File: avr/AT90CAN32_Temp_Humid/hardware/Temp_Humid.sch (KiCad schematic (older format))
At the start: 17 parts, among them P1 CONN_3X2, P2 CONN_4, P3 CONN_4, U1 DS1820, U2 AT90CAN32, U3 7805, U4 MCP2551, X1 16MHz

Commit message: Finilized HIH4000 humdity reading and reviewed PCB before paper print
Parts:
- removed P?: CONN_2, symbol CONN_2
- added K1: CONN_3, symbol CONN_3
- added SW1: SW_PUSH, symbol SW_PUSH
- added U5: HIH4000, symbol DS1820
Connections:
- wire segments 92 -> 114
- no-connect marks 49 -> 46
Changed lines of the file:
@@
 LIBS:contrib
 LIBS:valves
-LIBS:CAN_Temp-cache
+LIBS:Temp_Humid-cache
 EELAYER 27 0
 EELAYER END
@@
 Sheet 1 1
 Title ""
-Date "17 oct 2014"
+Date "20 oct 2014"
 Rev ""
 Comp ""
@@
 NoConn ~ 6500 3900
 NoConn ~ 6500 4000
-NoConn ~ 6500 4150
 NoConn ~ 6500 4250
 NoConn ~ 6500 4350
@@
 NoConn ~ 4550 4350
 NoConn ~ 4550 4250
-NoConn ~ 4550 4150
 NoConn ~ 4550 4000
 NoConn ~ 4550 3900
@@
 $EndComp
 $Comp
-L +5V #PWR01
+L +5V #PWR5
 U 1 1 00000000
 P 3450 1700
-F 0 "#PWR01" H 3450 1790 20  0001 C CNN
+F 0 "#PWR5" H 3450 1790 20  0001 C CNN
 F 1 "+5V" H 3450 1790 30  0000 C CNN
 F 2 "" H 3450 1700 60  0001 C CNN
@@
 $EndComp
 $Comp
-L GND #PWR02
+L GND #PWR2
 U 1 1 52152F91
 P 2850 2300
-F 0 "#PWR02" H 2850 2300 30  0001 C CNN
+F 0 "#PWR2" H 2850 2300 30  0001 C CNN
 F 1 "GND" H 2850 2230 30  0001 C CNN
 F 2 "" H 2850 2300 60  0001 C CNN
@@
 $EndComp
 $Comp
-L +5V #PWR03
+L +5V #PWR1
 U 1 1 52152F8D
 P 2600 3650
-F 0 "#PWR03" H 2600 3740 20  0001 C CNN
+F 0 "#PWR1" H 2600 3740 20  0001 C CNN
 F 1 "+5V" H 2600 3740 30  0000 C CNN
 F 2 "" H 2600 3650 60  0001 C CNN
@@
 $EndComp
 $Comp
-L GND #PWR04
+L GND #PWR4
 U 1 1 52152F8B
 P 3150 4350
-F 0 "#PWR04" H 3150 4350 30  0001 C CNN
+F 0 "#PWR4" H 3150 4350 30  0001 C CNN
 F 1 "GND" H 3150 4280 30  0001 C CNN
 F 2 "" H 3150 4350 60  0001 C CNN
@@
 $EndComp
 $Comp
-L +5V #PWR05
+L +5V #PWR6
 U 1 1 52152F8A
 P 3600 4000
-F 0 "#PWR05" H 3600 4090 20  0001 C CNN
+F 0 "#PWR6" H 3600 4090 20  0001 C CNN
 F 1 "+5V" H 3600 4090 30  0000 C CNN
 F 2 "" H 3600 4000 60  0001 C CNN
@@
 $EndComp
 $Comp
-L +5V #PWR06
+L +5V #PWR8
 U 1 1 52152F74
 P 5550 1750
-F 0 "#PWR06" H 5550 1840 20  0001 C CNN
+F 0 "#PWR8" H 5550 1840 20  0001 C CNN
 F 1 "+5V" H 5550 1840 30  0000 C CNN
 F 2 "" H 5550 1750 60  0001 C CNN
@@
 $EndComp
 $Comp
-L GND #PWR07
+L GND #PWR9
 U 1 1 52152F83
 P 5800 6250
-F 0 "#PWR07" H 5800 6250 30  0001 C CNN
+F 0 "#PWR9" H 5800 6250 30  0001 C CNN
 F 1 "GND" H 5800 6180 30  0001 C CNN
 F 2 "" H 5800 6250 60  0001 C CNN
 F 3 "" H 5800 6250 60  0001 C CNN
 	1    5800 6250
-	1    0    0    -1
-$EndComp
-NoConn ~ 8250 3850
-$Comp
-L GND #PWR08
-U 1 1 52152F82
-P 6950 4150
-F 0 "#PWR08" H 6950 4150 30  0001 C CNN
-F 1 "GND" H 6950 4080 30  0001 C CNN
-F 2 "" H 6950 4150 60  0001 C CNN
-F 3 "" H 6950 4150 60  0001 C CNN
-	1    6950 4150
 	1    0    0    -1
 $EndComp
@@
 $EndComp
 $Comp
-L +5V #PWR09
+L +5V #PWR10
 U 1 1 52152F7D
 P 6750 1150
-F 0 "#PWR09" H 6750 1240 20  0001 C CNN
+F 0 "#PWR10" H 6750 1240 20  0001 C CNN
 F 1 "+5V" H 6750 1240 30  0000 C CNN
 F 2 "" H 6750 1150 60  0001 C CNN
@@
 $EndComp
 $Comp
-L GND #PWR010
+L GND #PWR12
 U 1 1 52152F7C
 P 7700 1900
-F 0 "#PWR010" H 7700 1900 30  0001 C CNN
+F 0 "#PWR12" H 7700 1900 30  0001 C CNN
 F 1 "GND" H 7700 1830 30  0001 C CNN
 F 2 "" H 7700 1900 60  0001 C CNN
@@
 $EndComp
 $Comp
-L +12V #PWR011
+L +12V #PWR14
 U 1 1 52152F79
 P 8900 1050
-F 0 "#PWR011" H 8900 1000 20  0001 C CNN
+F 0 "#PWR14" H 8900 1000 20  0001 C CNN
 F 1 "+12V" H 8900 1150 30  0000 C CNN
 F 2 "" H 8900 1050 60  0001 C CNN
@@
 $EndComp
 $Comp
-L GND #PWR012
+L GND #PWR13
 U 1 1 52152F78
 P 8750 5050
-F 0 "#PWR012" H 8750 5050 30  0001 C CNN
+F 0 "#PWR13" H 8750 5050 30  0001 C CNN
 F 1 "GND" H 8750 4980 30  0001 C CNN
 F 2 "" H 8750 5050 60  0001 C CNN
@@
 	3000 2050 3000 1900
 Wire Wire Line
-	3100 2450 4550 2450
-Wire Wire Line
 	3900 4550 3750 4550
 Connection ~ 3050 4700
@@
 	2600 3650 2600 3950
 Wire Wire Line
-	3100 2450 3100 1900
+	3100 1900 3100 2750
 Wire Wire Line
 	3200 1900 3200 2050
@@
 Wire Wire Line
 	3700 2350 3700 2450
-Connection ~ 3700 2450
 Wire Wire Line
 	5800 5950 5800 6250
@@
 	8100 1300 8100 1250
 $Comp
-L GND #PWR013
+L GND #PWR3
 U 1 1 52BCB805
 P 2900 5750
-F 0 "#PWR013" H 2900 5750 30  0001 C CNN
+F 0 "#PWR3" H 2900 5750 30  0001 C CNN
 F 1 "GND" H 2900 5680 30  0001 C CNN
 F 2 "" H 2900 5750 60  0000 C CNN
@@
 	2900 3850 2600 3850
 Connection ~ 2600 3850
-$Comp
-L CONN_2 P?
-U 1 1 544180F6
+NoConn ~ 6500 2850
+Wire Wire Line
+	6850 2750 6500 2750
+Wire Wire Line
+	6800 2650 6500 2650
+Wire Wire Line
+	8250 3850 8400 3850
+Wire Wire Line
+	8400 3850 8400 4750
+Wire Wire Line
+	8400 4750 8750 4750
+Connection ~ 8750 4750
+Wire Wire Line
+	6950 4150 8400 4150
+Connection ~ 8400 4150
+Wire Wire Line
+	4550 4150 3950 4150
+Wire Wire Line
+	3950 4150 3950 2750
+Wire Wire Line
+	3950 2750 3100 2750
+$Comp
+L SW_PUSH SW1
+U 1 1 54418504
+P 4250 2050
+F 0 "SW1" H 4400 2160 50  0000 C CNN
+F 1 "SW_PUSH" H 4250 1970 50  0000 C CNN
+F 2 "" H 4250 2050 60  0000 C CNN
+F 3 "" H 4250 2050 60  0000 C CNN
+	1    4250 2050
+	0    -1   -1   0
+$EndComp
+$Comp
+L GND #PWR7
+U 1 1 54418511
+P 4650 1800
+F 0 "#PWR7" H 4650 1800 30  0001 C CNN
+F 1 "GND" H 4650 1730 30  0001 C CNN
+F 2 "" H 4650 1800 60  0001 C CNN
+F 3 "" H 4650 1800 60  0001 C CNN
+	1    4650 1800
+	1    0    0    -1
+$EndComp
+Wire Wire Line
+	4550 2450 4250 2450
+Wire Wire Line
+	4250 2450 4250 2350
+Wire Wire Line
+	4250 1750 4250 1550
+Wire Wire Line
+	4250 1550 4650 1550
+Wire Wire Line
+	4650 1550 4650 1800
+Wire Wire Line
+	3700 2450 3100 2450
+Connection ~ 3100 2450
+$Comp
+L DS1820 U5
+U 1 1 54456AA5
+P 7250 5000
+F 0 "U5" H 7250 4300 60  0000 C CNN
+F 1 "HIH4000" H 7250 5000 60  0000 C CNN
+F 2 "" H 7250 5000 60  0000 C CNN
+F 3 "" H 7250 5000 60  0000 C CNN
+	1    7250 5000
+	-1   0    0    1
+$EndComp
+Wire Wire Line
+	6500 4150 6850 4150
+Wire Wire Line
+	6850 4150 6850 4300
+Wire Wire Line
+	6850 4300 7250 4300
+Wire Wire Line
+	7250 4300 7250 4450
+Wire Wire Line
+	7350 4450 8400 4450
+Connection ~ 8400 4450
+$Comp
+L +5V #PWR11
+U 1 1 54456BCE
+P 6800 4600
+F 0 "#PWR11" H 6800 4690 20  0001 C CNN
+F 1 "+5V" H 6800 4690 30  0000 C CNN
+F 2 "" H 6800 4600 60  0001 C CNN
+F 3 "" H 6800 4600 60  0001 C CNN
+	1    6800 4600
+	1    0    0    -1
+$EndComp
+Wire Wire Line
+	7150 4450 6950 4450
+Wire Wire Line
+	6950 4450 6950 4750
+Wire Wire Line
+	6950 4750 6800 4750
+Wire Wire Line
+	6800 4750 6800 4600
+$Comp
+L CONN_3 K1
+U 1 1 544570D5
 P 7500 2550
-F 0 "P?" V 7450 2550 40  0000 C CNN
-F 1 "CONN_2" V 7550 2550 40  0000 C CNN
+F 0 "K1" V 7450 2550 50  0000 C CNN
+F 1 "CONN_3" V 7550 2550 40  0000 C CNN
 F 2 "" H 7500 2550 60  0000 C CNN
 F 3 "" H 7500 2550 60  0000 C CNN
@@
 $EndComp
 Wire Wire Line
-	6800 2450 7150 2450
-Wire Wire Line
-	6850 2650 7150 2650
-NoConn ~ 6500 2850
+	7150 2650 6850 2650
 Wire Wire Line
 	6850 2650 6850 2750
 Wire Wire Line
-	6850 2750 6500 2750
-Wire Wire Line
-	6800 2450 6800 2650
-Wire Wire Line
-	6800 2650 6500 2650
+	7150 2550 6800 2550
+Wire Wire Line
+	6800 2550 6800 2650
+Wire Wire Line
+	7150 2450 7150 1700
+Connection ~ 7150 1700
 $EndSCHEMATC

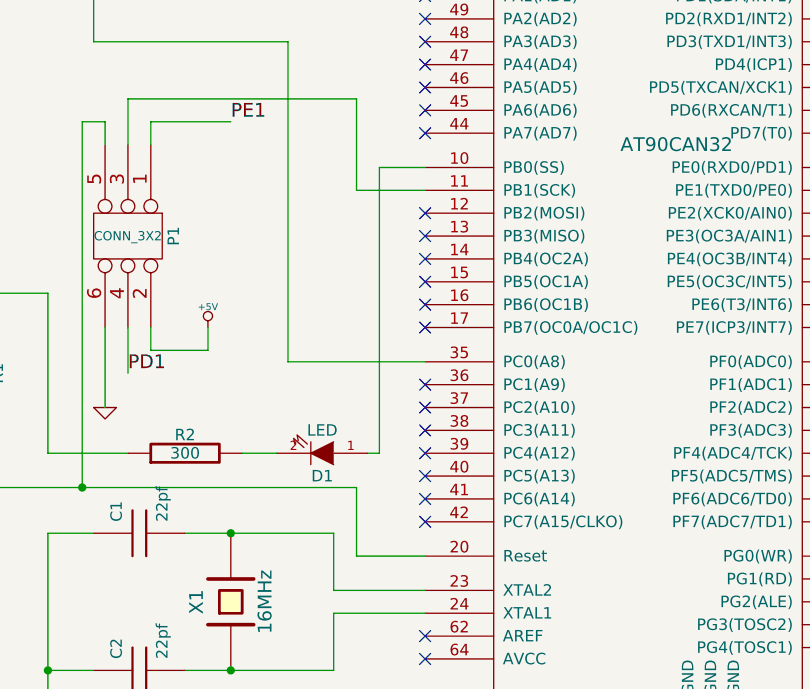
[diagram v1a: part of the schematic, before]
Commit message: Updating PCB before footprint test on paper printout
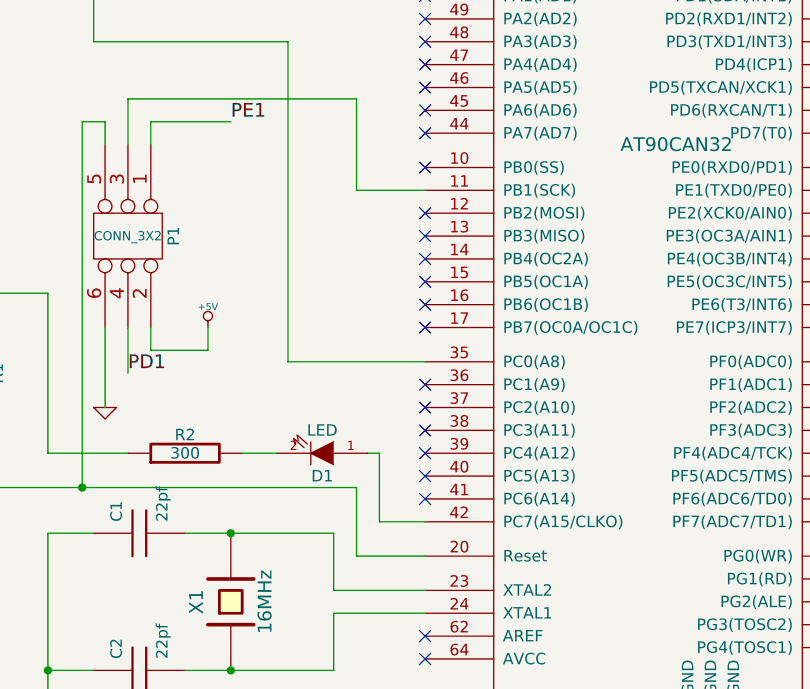
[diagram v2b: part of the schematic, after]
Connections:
- net at U2.10 (PB0(SS)): no longer D1.1 (A)
- net at U2.42 (PC7(A15/CLKO)): now also D1.1 (A)
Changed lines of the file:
@@
 Sheet 1 1
 Title ""
-Date "20 oct 2014"
+Date "21 oct 2014"
 Rev ""
 Comp ""
@@
 NoConn ~ 4550 5450
 NoConn ~ 4550 5350
-NoConn ~ 4550 4850
 NoConn ~ 4550 4750
 NoConn ~ 4550 4650
@@
 $EndComp
 $Comp
-L +5V #PWR5
+L +5V #PWR01
 U 1 1 00000000
 P 3450 1700
-F 0 "#PWR5" H 3450 1790 20  0001 C CNN
+F 0 "#PWR01" H 3450 1790 20  0001 C CNN
 F 1 "+5V" H 3450 1790 30  0000 C CNN
 F 2 "" H 3450 1700 60  0001 C CNN
@@
 $EndComp
 $Comp
-L GND #PWR2
+L GND #PWR02
 U 1 1 52152F91
 P 2850 2300
-F 0 "#PWR2" H 2850 2300 30  0001 C CNN
+F 0 "#PWR02" H 2850 2300 30  0001 C CNN
 F 1 "GND" H 2850 2230 30  0001 C CNN
 F 2 "" H 2850 2300 60  0001 C CNN
@@
 $EndComp
 $Comp
-L +5V #PWR1
+L +5V #PWR03
 U 1 1 52152F8D
 P 2600 3650
-F 0 "#PWR1" H 2600 3740 20  0001 C CNN
+F 0 "#PWR03" H 2600 3740 20  0001 C CNN
 F 1 "+5V" H 2600 3740 30  0000 C CNN
 F 2 "" H 2600 3650 60  0001 C CNN
@@
 $EndComp
 $Comp
-L GND #PWR4
+L GND #PWR04
 U 1 1 52152F8B
 P 3150 4350
-F 0 "#PWR4" H 3150 4350 30  0001 C CNN
+F 0 "#PWR04" H 3150 4350 30  0001 C CNN
 F 1 "GND" H 3150 4280 30  0001 C CNN
 F 2 "" H 3150 4350 60  0001 C CNN
@@
 $EndComp
 $Comp
-L +5V #PWR6
+L +5V #PWR05
 U 1 1 52152F8A
 P 3600 4000
-F 0 "#PWR6" H 3600 4090 20  0001 C CNN
+F 0 "#PWR05" H 3600 4090 20  0001 C CNN
 F 1 "+5V" H 3600 4090 30  0000 C CNN
 F 2 "" H 3600 4000 60  0001 C CNN
@@
 $EndComp
 $Comp
-L +5V #PWR8
+L +5V #PWR06
 U 1 1 52152F74
 P 5550 1750
-F 0 "#PWR8" H 5550 1840 20  0001 C CNN
+F 0 "#PWR06" H 5550 1840 20  0001 C CNN
 F 1 "+5V" H 5550 1840 30  0000 C CNN
 F 2 "" H 5550 1750 60  0001 C CNN
@@
 $EndComp
 $Comp
-L GND #PWR9
+L GND #PWR07
 U 1 1 52152F83
 P 5800 6250
-F 0 "#PWR9" H 5800 6250 30  0001 C CNN
+F 0 "#PWR07" H 5800 6250 30  0001 C CNN
 F 1 "GND" H 5800 6180 30  0001 C CNN
 F 2 "" H 5800 6250 60  0001 C CNN
@@
 $EndComp
 $Comp
-L +5V #PWR10
+L +5V #PWR08
 U 1 1 52152F7D
 P 6750 1150
-F 0 "#PWR10" H 6750 1240 20  0001 C CNN
+F 0 "#PWR08" H 6750 1240 20  0001 C CNN
 F 1 "+5V" H 6750 1240 30  0000 C CNN
 F 2 "" H 6750 1150 60  0001 C CNN
@@
 $EndComp
 $Comp
-L GND #PWR12
+L GND #PWR09
 U 1 1 52152F7C
 P 7700 1900
-F 0 "#PWR12" H 7700 1900 30  0001 C CNN
+F 0 "#PWR09" H 7700 1900 30  0001 C CNN
 F 1 "GND" H 7700 1830 30  0001 C CNN
 F 2 "" H 7700 1900 60  0001 C CNN
@@
 $EndComp
 $Comp
-L +12V #PWR14
+L +12V #PWR010
 U 1 1 52152F79
 P 8900 1050
-F 0 "#PWR14" H 8900 1000 20  0001 C CNN
+F 0 "#PWR010" H 8900 1000 20  0001 C CNN
 F 1 "+12V" H 8900 1150 30  0000 C CNN
 F 2 "" H 8900 1050 60  0001 C CNN
@@
 $EndComp
 $Comp
-L GND #PWR13
+L GND #PWR011
 U 1 1 52152F78
 P 8750 5050
-F 0 "#PWR13" H 8750 5050 30  0001 C CNN
+F 0 "#PWR011" H 8750 5050 30  0001 C CNN
 F 1 "GND" H 8750 4980 30  0001 C CNN
 F 2 "" H 8750 5050 60  0001 C CNN
@@
 	8100 1300 8100 1250
 $Comp
-L GND #PWR3
+L GND #PWR012
 U 1 1 52BCB805
 P 2900 5750
-F 0 "#PWR3" H 2900 5750 30  0001 C CNN
+F 0 "#PWR012" H 2900 5750 30  0001 C CNN
 F 1 "GND" H 2900 5680 30  0001 C CNN
 F 2 "" H 2900 5750 60  0000 C CNN
@@
 	1    0    0    -1
 $EndComp
-Wire Wire Line
-	4550 3300 4350 3300
-Wire Wire Line
-	4350 3300 4350 4550
 Wire Wire Line
 	4350 4550 4300 4550
@@
 $EndComp
 $Comp
-L GND #PWR7
+L GND #PWR013
 U 1 1 54418511
 P 4650 1800
-F 0 "#PWR7" H 4650 1800 30  0001 C CNN
+F 0 "#PWR013" H 4650 1800 30  0001 C CNN
 F 1 "GND" H 4650 1730 30  0001 C CNN
 F 2 "" H 4650 1800 60  0001 C CNN
@@
 Connection ~ 8400 4450
 $Comp
-L +5V #PWR11
+L +5V #PWR014
 U 1 1 54456BCE
 P 6800 4600
-F 0 "#PWR11" H 6800 4690 20  0001 C CNN
+F 0 "#PWR014" H 6800 4690 20  0001 C CNN
 F 1 "+5V" H 6800 4690 30  0000 C CNN
 F 2 "" H 6800 4600 60  0001 C CNN
@@
 	7150 2450 7150 1700
 Connection ~ 7150 1700
+Wire Wire Line
+	4550 4850 4350 4850
+Wire Wire Line
+	4350 4850 4350 4550
+NoConn ~ 4550 3300
 $EndSCHEMATC

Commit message: Last update on PCB before ordering
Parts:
- removed P2, P3: CONN_4, symbol CONN_4
- added C5, C6: 100nF, symbol C
- added U6: RJ45_DUAL, ~, symbol RJ45_DUAL
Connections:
- net +12V: now also U6.1, U6.10, U6.11, U6.2, U6.3, U6.9
- net +5V: now also C5.1, C6.2
- net GND: now also C5.2, C6.1, U6.14, U6.15, U6.16, U6.6, U6.7, U6.8
- net at U4.6 (CANL): now also U6.13, U6.5
- net at U4.7 (CANH): now also U6.12, U6.4
- no-connect marks 46 -> 48
